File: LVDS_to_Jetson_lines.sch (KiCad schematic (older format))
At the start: 22 parts, among them U2 SN74AVC2T45DCUR, U5 TS3DDR3812_RUA_42, U6 TS3DDR3812_RUA_42, U8 SN74AVCH16T245_DGV_48

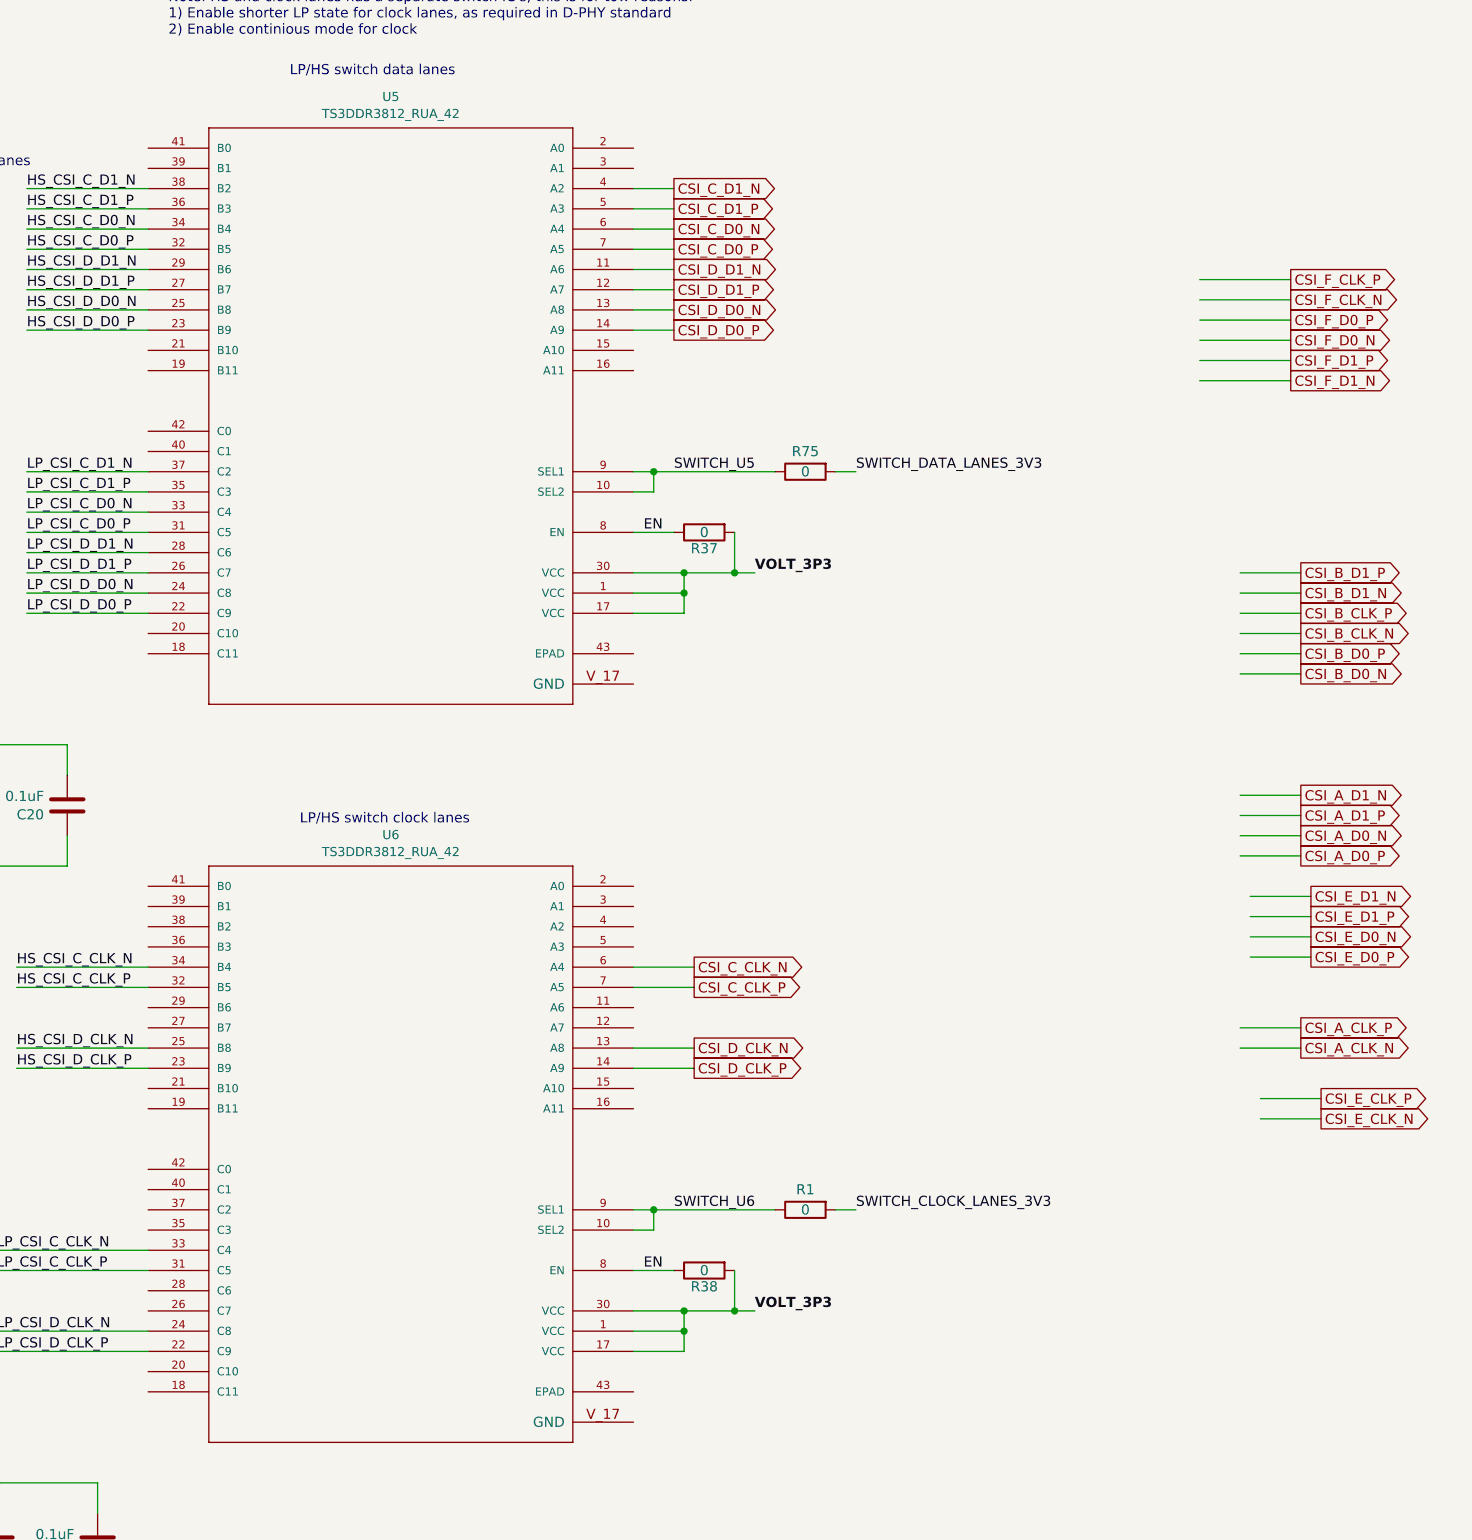
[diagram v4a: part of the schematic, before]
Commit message: Adding more LVDS lines
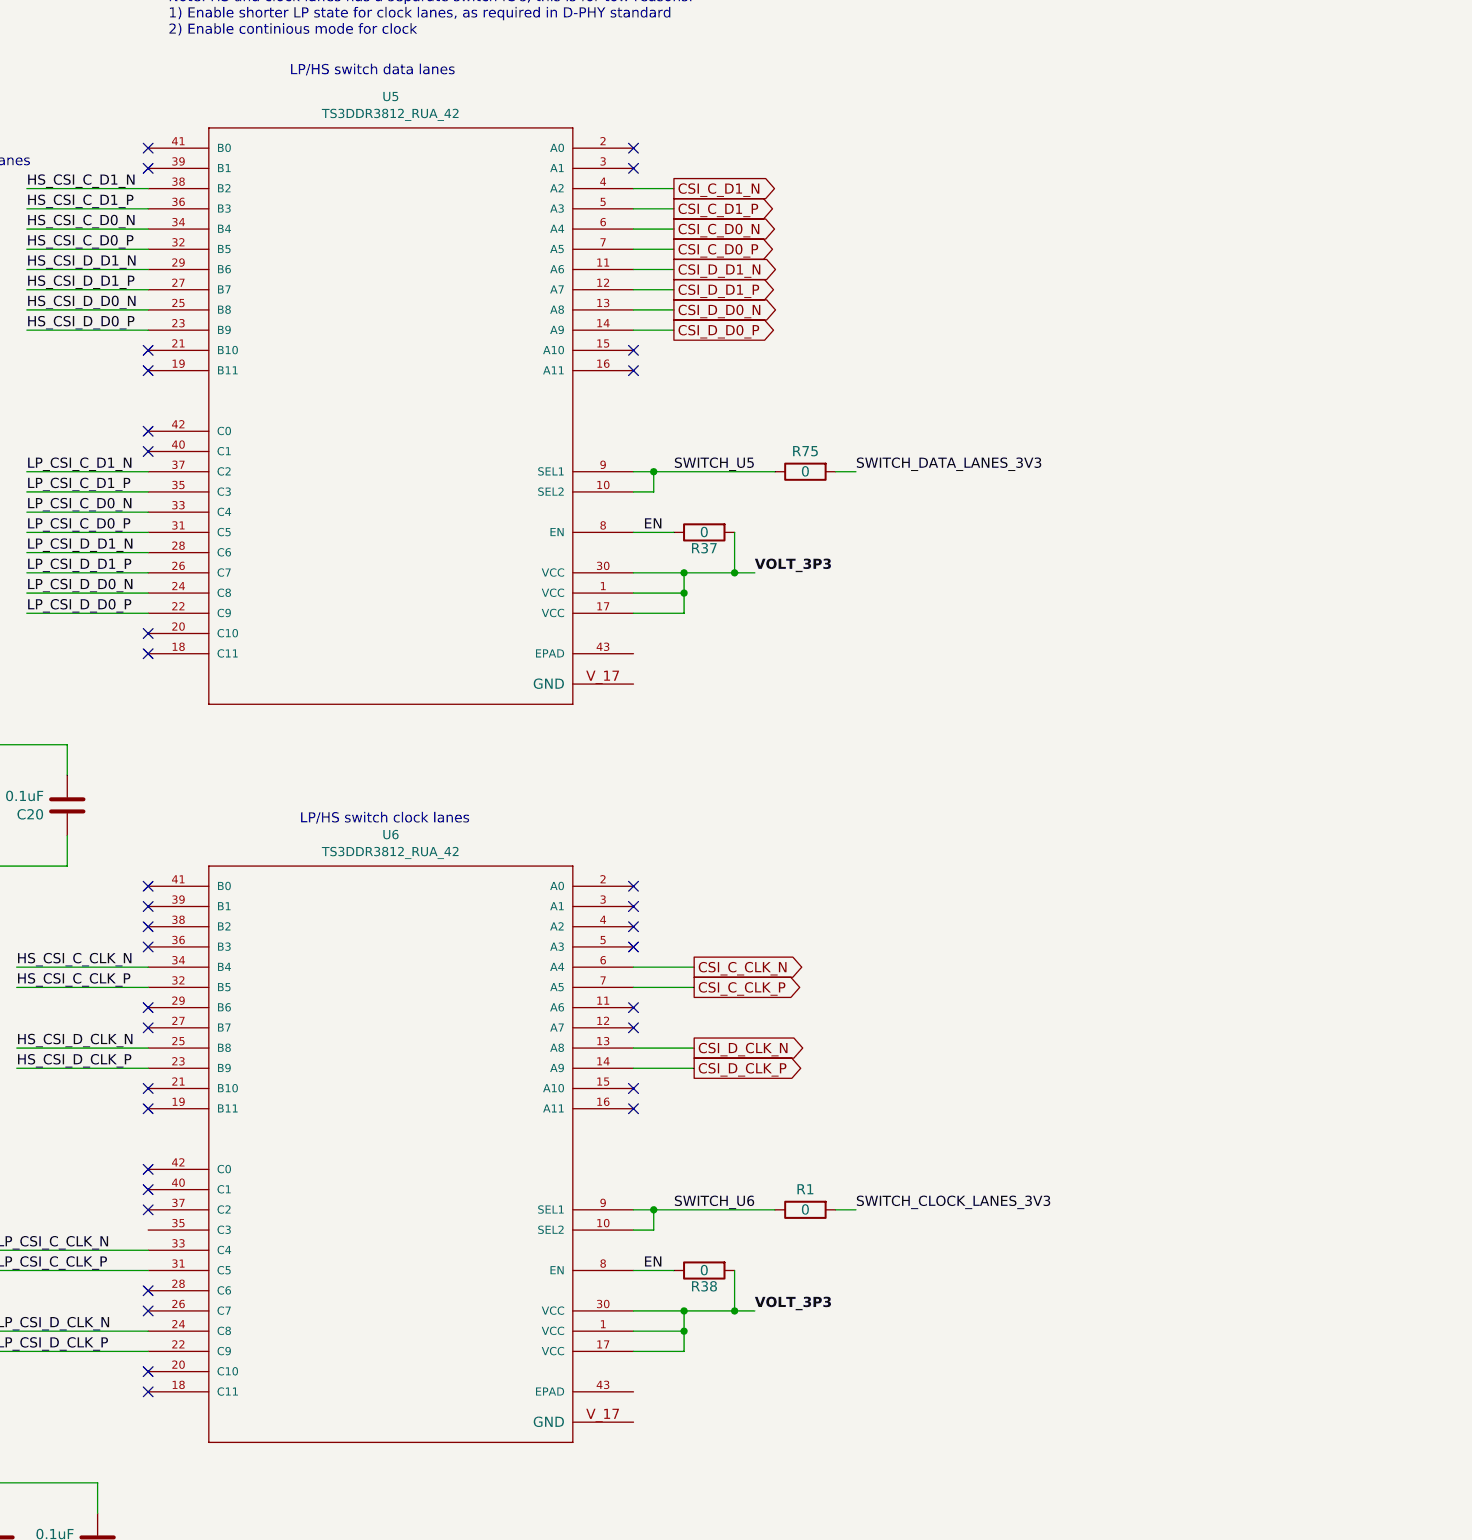
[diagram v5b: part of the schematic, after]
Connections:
- net labels removed: CSI_A_CLK_N, CSI_A_CLK_P, CSI_A_D0_N, CSI_A_D0_P, CSI_A_D1_N, CSI_A_D1_P, CSI_B_CLK_N, CSI_B_CLK_P, CSI_B_D0_N, CSI_B_D0_P, CSI_B_D1_N, CSI_B_D1_P, CSI_E_CLK_N, CSI_E_CLK_P, CSI_E_D0_N, CSI_E_D0_P, CSI_E_D1_N, CSI_E_D1_P, CSI_F_CLK_N, CSI_F_CLK_P, CSI_F_D0_N, CSI_F_D0_P, CSI_F_D1_N, CSI_F_D1_P
- wire segments 270 -> 246
- no-connect marks 0 -> 35
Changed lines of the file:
@@
 $Descr A3 16535 11693
 encoding utf-8
-Sheet 4 12
+Sheet 4 19
 Title ""
 Date ""
@@
 Text GLabel 14750 7000 2    50   Output ~ 0
 CSI_D_CLK_N
-Text GLabel 17700 3400 2    50   Output ~ 0
-CSI_F_D0_P
-Text GLabel 17700 3500 2    50   Output ~ 0
-CSI_F_D0_N
-Text GLabel 17700 3200 2    50   Output ~ 0
-CSI_F_CLK_P
-Text GLabel 17700 3300 2    50   Output ~ 0
-CSI_F_CLK_N
-Text GLabel 17700 3600 2    50   Output ~ 0
-CSI_F_D1_P
-Text GLabel 17700 3700 2    50   Output ~ 0
-CSI_F_D1_N
-Text GLabel 17800 6550 2    50   Output ~ 0
-CSI_E_D0_P
-Text GLabel 17800 6450 2    50   Output ~ 0
-CSI_E_D0_N
-Text GLabel 17850 7250 2    50   Output ~ 0
-CSI_E_CLK_P
-Text GLabel 17850 7350 2    50   Output ~ 0
-CSI_E_CLK_N
-Text GLabel 17800 6350 2    50   Output ~ 0
-CSI_E_D1_P
-Text GLabel 17800 6250 2    50   Output ~ 0
-CSI_E_D1_N
 Wire Wire Line
 	14450 6700 14750 6700
 Wire Wire Line
 	14450 6600 14750 6600
-Wire Wire Line
-	17250 3200 17700 3200
-Wire Wire Line
-	17250 3300 17700 3300
-Wire Wire Line
-	17250 3400 17700 3400
-Wire Wire Line
-	17250 3500 17700 3500
-Wire Wire Line
-	17250 3600 17700 3600
-Wire Wire Line
-	17250 3700 17700 3700
-Text GLabel 17750 5950 2    50   Output ~ 0
-CSI_A_D0_N
-Text GLabel 17750 7000 2    50   Output ~ 0
-CSI_A_CLK_N
-Text GLabel 17750 6900 2    50   Output ~ 0
-CSI_A_CLK_P
-Text GLabel 17750 5750 2    50   Output ~ 0
-CSI_A_D1_N
-Text GLabel 17750 5850 2    50   Output ~ 0
-CSI_A_D1_P
-Text GLabel 17750 5150 2    50   Output ~ 0
-CSI_B_D0_N
-Text GLabel 17750 5050 2    50   Output ~ 0
-CSI_B_D0_P
-Text GLabel 17750 4950 2    50   Output ~ 0
-CSI_B_CLK_N
-Text GLabel 17750 4850 2    50   Output ~ 0
-CSI_B_CLK_P
-Text GLabel 17750 4750 2    50   Output ~ 0
-CSI_B_D1_N
-Text GLabel 17750 4650 2    50   Output ~ 0
-CSI_B_D1_P
-Wire Wire Line
-	17450 4950 17750 4950
-Wire Wire Line
-	17450 4850 17750 4850
-Wire Wire Line
-	17450 5150 17750 5150
-Wire Wire Line
-	17450 5050 17750 5050
-Wire Wire Line
-	17450 4750 17750 4750
-Wire Wire Line
-	17450 4650 17750 4650
-Wire Wire Line
-	17500 6450 17800 6450
-Wire Wire Line
-	17500 6550 17800 6550
-Wire Wire Line
-	17500 6250 17800 6250
-Wire Wire Line
-	17500 6350 17800 6350
-Wire Wire Line
-	17450 5750 17750 5750
-Wire Wire Line
-	17450 5850 17750 5850
-Wire Wire Line
-	17450 5950 17750 5950
-Wire Wire Line
-	17450 6050 17750 6050
-Text GLabel 17750 6050 2    50   Output ~ 0
-CSI_A_D0_P
 $Comp
 L FMC_MIPI_v2:TS3DDR3812_RUA_42 U?
@@
 	1    0    0    -1
 $EndComp
-Wire Wire Line
-	17550 7250 17850 7250
-Wire Wire Line
-	17550 7350 17850 7350
-Wire Wire Line
-	17450 6900 17750 6900
-Wire Wire Line
-	17450 7000 17750 7000
 Text Notes 3950 1450 0    157  ~ 31
 NOTE: use CSI A and CSI B from the same IC, since they can form 4 lane configuration\n
@@
 Wire Wire Line
 	1750 2650 2200 2650
+NoConn ~ 12050 2550
+NoConn ~ 12050 2650
+NoConn ~ 12050 3550
+NoConn ~ 12050 3650
+NoConn ~ 14450 2550
+NoConn ~ 14450 2650
+NoConn ~ 14450 3550
+NoConn ~ 14450 3650
+NoConn ~ 12050 3950
+NoConn ~ 12050 4050
+NoConn ~ 12050 4950
+NoConn ~ 12050 5050
+NoConn ~ 12050 6200
+NoConn ~ 12050 6300
+NoConn ~ 12050 6400
+NoConn ~ 12050 6500
+NoConn ~ 12050 6800
+NoConn ~ 12050 6900
+NoConn ~ 12050 7200
+NoConn ~ 12050 7300
+NoConn ~ 14450 6200
+NoConn ~ 14450 6300
+NoConn ~ 14450 6400
+NoConn ~ 14450 6500
+NoConn ~ 14450 6800
+NoConn ~ 14450 6900
+NoConn ~ 14450 7200
+NoConn ~ 14450 7300
+NoConn ~ 12050 7600
+NoConn ~ 12050 7700
+NoConn ~ 12050 7800
+NoConn ~ 12050 8200
+NoConn ~ 12050 8300
+NoConn ~ 12050 8600
+NoConn ~ 12050 8700
 $EndSCHEMATC

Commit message: added 4 bit level shifter VADJ to 3.3 volt
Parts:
- removed U2: SN74AVC2T45DCUR, FMC_MIPI_v2_sym:SN74AVC2T45DCUR, symbol FMC_MIPI_v2:SN74AVC2T45DCUR
- added IC1: SN74AVC4T245PWR, SOP65P640X120-16N, symbol FMC_MIPI_v2:SN74AVC4T245PWR
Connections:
- net Earth: now also IC1.14 (2~OE), IC1.15 (1~OE), IC1.8 (GND), IC1.9 (GND)
- net FMC_SWITCH_CLOCK_LANES_VADJ: now also IC1.5 (1A2)
- net FMC_SWITCH_DATA_LANES_VADJ: now also IC1.4 (1A1)
- net SWITCH_CLOCK_LANES_3V3: now also IC1.12 (1B2)
- net SWITCH_DATA_LANES_3V3: now also IC1.13 (1B1)
- net VDD_VADJ: now also IC1.1 (VCCA)
- net VOLT_3P3: now also IC1.16 (VCCB); no longer R37.2, R38.2
- net DIR_U2 renamed DIR_IC1
- net DIR_IC1: now also IC1.2 (1DIR), IC1.3 (2DIR)
- net EN renamed EN_U5
- net EN_U5: no longer R38.1, U6.8 (EN)
- new net EN_MIPI_OUT_CLOCK_3V3: IC1.10 (2B2), R38.2
- new net EN_MIPI_OUT_DATA_3V3: IC1.11 (2B1), R37.2
- new net EN_U6: R38.1, U6.8 (EN)
- new net FMC_EN_MIPI_OUT_CLOCK_VADJ: IC1.7 (2A2)
- new net FMC_EN_MIPI_OUT_DATA_VADJ: IC1.6 (2A1)
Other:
- note added: "Decoupling capacitors IC1"
- note added: "TODO:!! Use 4 bit level shifter to 3.3 volt, \nuse output enable pin as well.\nUSE: SN74AVC4T245PWR"
- note removed: "Decoupling capacitors U2"
- note removed: "NOTE: use CSI A and CSI B from the same IC, since they can form 4 lane configuration\n"
- moved on the sheet: C1, C2, R2, R38
